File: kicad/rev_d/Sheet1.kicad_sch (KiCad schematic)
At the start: 159 parts, among them J1 JUMPER, J2 JUMPER, J3 JUMPER, J4 JUMPER, J7 JUMPER, Q1 QUARTZ, X1 FDD34M, X2 IDE40M, X3 IDC26LPT, X7 DB15VGA, X8 PLB1-4I, X9 PLB1-2

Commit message: pentevo: small update to converted kicad sch (resistors, capacitors, regulators, glue logic)
git-svn-id: svn://localhost/local-pentevo@1170 c6c76956-fad2-4150-a3a9-ea0a427205ba
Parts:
- D19: value 138 -> '138
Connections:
- net GND: now also C102.2, C103.2, C104.2, C70.2, C71.2, C79.2, C80.2, C95.2, R54.1 (i/o), R59.1 (i/o)
- net IORQGE1: now also R58.2 (i/o1)
- net IORQGE2: now also R59.2 (i/o1)
- net VCC12S: now also J4.1 (2)
- net VCC2V5: now also C28.1, C79.1, C80.1
- net VCC3V3: now also C26.1, C70.1, C71.1
- net VCC5: now also C25.1, C27.1, R48.1 (i/o), R49.1 (i/o), R51.1 (i/o), R52.1 (i/o), R64.1 (i/o)
- net ~{BUSR}: now also R53.2 (i/o1)
- net ~{CSROM}: now also R56.2 (i/o1)
- net ~{MREQ}: now also R49.2 (i/o1)
- net at C101.4: no longer C103.2
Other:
- moved on the sheet: C100, C101, C102, C95, C96, C97, C98, C99, J4, R96

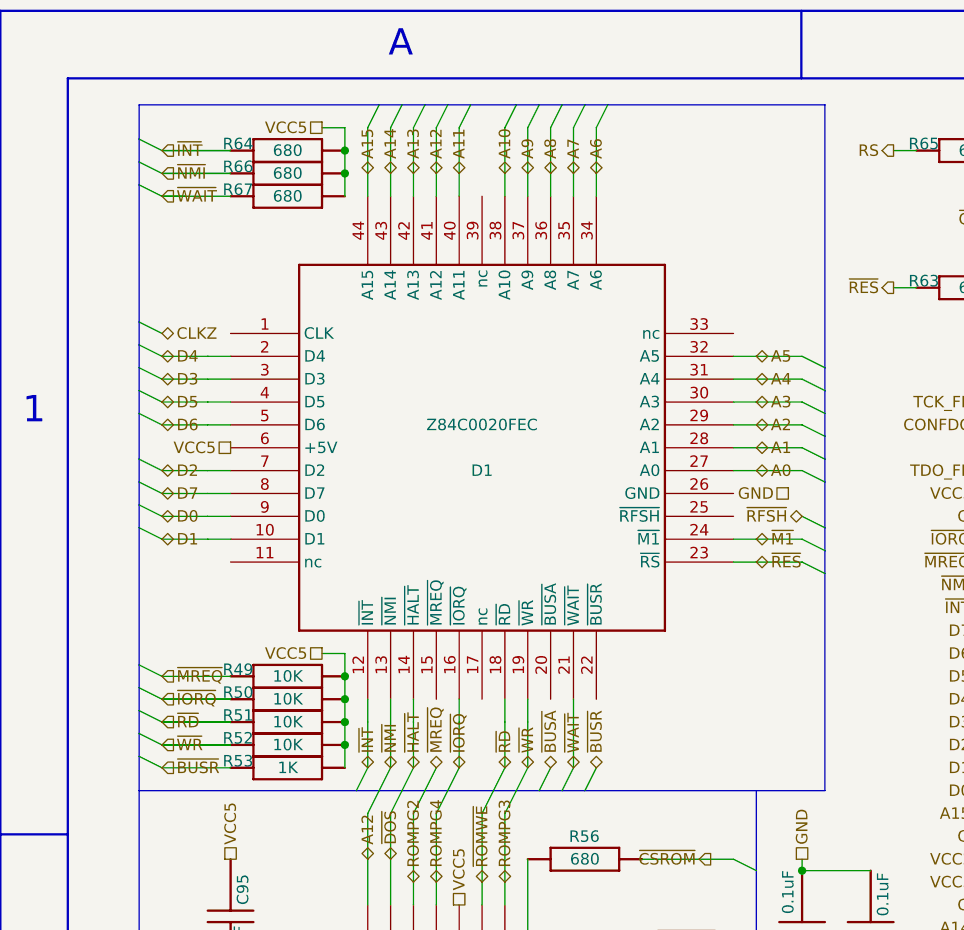
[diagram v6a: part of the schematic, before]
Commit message: pentevo: small update to converted kicad sch (Z80)
git-svn-id: svn://localhost/local-pentevo@1171 c6c76956-fad2-4150-a3a9-ea0a427205ba
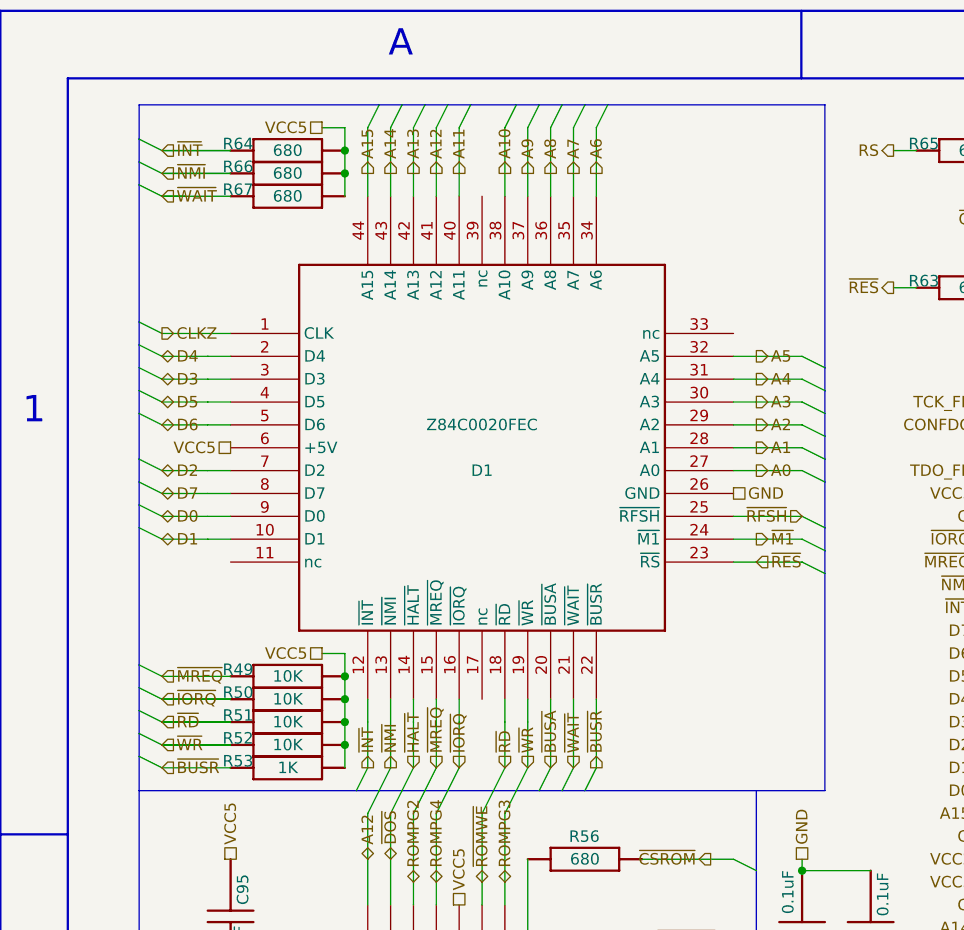
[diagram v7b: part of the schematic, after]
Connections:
- net CLKZ: now also D1.1 (CLK)
- net GND: now also D1.26 (GND)
- net ~{BUSA}: now also D1.20 (~{BUSA})
- net ~{BUSR}: now also D1.22 (~{BUSR})
- net ~{MREQ}: now also D1.15 (~{MREQ})
- net ~{RFSH}: now also D1.25 (~{RFSH})
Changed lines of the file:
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@@
 	(wire
 		(pts
+			(xy 71.12 124.46) (xy 71.12 132.08)
+		)
+		(stroke
+			(width 0)
+			(type default)
+		)
+	)
+	(wire
+		(pts
 			(xy 381 276.86) (xy 388.62 276.86)
 		)
@@
 	(wire
 		(pts
+			(xy 58.42 124.46) (xy 58.42 132.08)
+		)
+		(stroke
+			(width 0)
+			(type default)
+		)
+	)
+	(wire
+		(pts
 			(xy 63.5 322.58) (xy 68.58 322.58)
 		)
@@
 		)
 	)
+	(wire
+		(pts
+			(xy 91.44 104.14) (xy 99.06 104.14)
+		)
+		(stroke
+			(width 0)
+			(type default)
+		)
+	)
 	(bus
 		(pts
@@
 	(wire
 		(pts
+			(xy 76.2 124.46) (xy 76.2 132.08)
+		)
+		(stroke
+			(width 0)
+			(type default)
+		)
+	)
+	(wire
+		(pts
 			(xy 212.09 260.35) (xy 207.01 260.35)
 		)
@@
 	(wire
 		(pts
+			(xy 27.94 83.82) (xy 35.56 83.82)
+		)
+		(stroke
+			(width 0)
+			(type default)
+		)
+	)
+	(wire
+		(pts
 			(xy 241.3 127) (xy 246.38 127)
 		)
@@
 	)
 	(hierarchical_label "A0"
-		(shape bidirectional)
+		(shape output)
 		(at 93.98 99.06 0)
 		(fields_autoplaced yes)
@@
 	)
 	(hierarchical_label "A15"
-		(shape bidirectional)
+		(shape output)
 		(at 50.8 66.04 90)
 		(fields_autoplaced yes)
@@
 	)
 	(hierarchical_label "~{HALT}"
-		(shape bidirectional)
+		(shape input)
 		(at 55.88 132.08 90)
 		(fields_autoplaced yes)
@@
 	)
 	(hierarchical_label "A13"
-		(shape bidirectional)
+		(shape output)
 		(at 55.88 66.04 90)
 		(fields_autoplaced yes)
@@
 	)
 	(hierarchical_label "A4"
-		(shape bidirectional)
+		(shape output)
 		(at 93.98 88.9 0)
 		(fields_autoplaced yes)
@@
 	)
 	(hierarchical_label "~{BUSA}"
-		(shape bidirectional)
+		(shape input)
 		(at 71.12 132.08 90)
 		(fields_autoplaced yes)
@@
 	)
 	(hierarchical_label "~{M1}"
-		(shape bidirectional)
+		(shape output)
 		(at 93.98 106.68 0)
 		(fields_autoplaced yes)
@@
 	)
 	(hierarchical_label "A9"
-		(shape bidirectional)
+		(shape output)
 		(at 68.58 66.04 90)
 		(fields_autoplaced yes)
@@
 	)
 	(hierarchical_label "A3"
-		(shape bidirectional)
+		(shape output)
 		(at 93.98 91.44 0)
 		(fields_autoplaced yes)
@@
 	)
 	(hierarchical_label "~{INT}"
-		(shape bidirectional)
+		(shape output)
 		(at 50.8 132.08 90)
 		(fields_autoplaced yes)
@@
 	)
 	(hierarchical_label "A7"
-		(shape bidirectional)
+		(shape output)
 		(at 73.66 66.04 90)
 		(fields_autoplaced yes)
@@
 	)
 	(hierarchical_label "~{WR}"
-		(shape bidirectional)
+		(shape input)
 		(at 68.58 132.08 90)
 		(fields_autoplaced yes)
@@
 	)
 	(hierarchical_label "~{BUSR}"
-		(shape bidirectional)
+		(shape output)
 		(at 76.2 132.08 90)
 		(fields_autoplaced yes)
@@
 	)
 	(hierarchical_label "~{MREQ}"
-		(shape bidirectional)
+		(shape input)
 		(at 58.42 132.08 90)
 		(fields_autoplaced yes)
@@
 	)
 	(hierarchical_label "A6"
-		(shape bidirectional)
+		(shape output)
 		(at 76.2 66.04 90)
 		(fields_autoplaced yes)
@@
 	)
 	(hierarchical_label "~{RFSH}"
-		(shape bidirectional)
+		(shape input)
 		(at 99.06 104.14 180)
 		(fields_autoplaced yes)
@@
 	)
 	(hierarchical_label "A2"
-		(shape bidirectional)
+		(shape output)
 		(at 93.98 93.98 0)
 		(fields_autoplaced yes)
@@
 	)
 	(hierarchical_label "A12"
-		(shape bidirectional)
+		(shape output)
 		(at 58.42 66.04 90)
 		(fields_autoplaced yes)
@@
 	)
 	(hierarchical_label "A5"
-		(shape bidirectional)
+		(shape output)
 		(at 93.98 86.36 0)
 		(fields_autoplaced yes)
@@
 	)
 	(hierarchical_label "CLKZ"
-		(shape bidirectional)
+		(shape output)
 		(at 27.94 83.82 0)
 		(fields_autoplaced yes)
@@
 	)
 	(hierarchical_label "~{NMI}"
-		(shape bidirectional)
+		(shape output)
 		(at 53.34 132.08 90)
 		(fields_autoplaced yes)
@@
 	)
 	(hierarchical_label "~{WAIT}"
-		(shape bidirectional)
+		(shape input)
 		(at 73.66 132.08 90)
 		(fields_autoplaced yes)
@@
 	)
 	(hierarchical_label "A8"
-		(shape bidirectional)
+		(shape output)
 		(at 71.12 66.04 90)
 		(fields_autoplaced yes)
@@
 	)
 	(hierarchical_label "A10"
-		(shape bidirectional)
+		(shape output)
 		(at 66.04 66.04 90)
 		(fields_autoplaced yes)
@@
 	)
 	(hierarchical_label "A1"
-		(shape bidirectional)
+		(shape output)
 		(at 93.98 96.52 0)
 		(fields_autoplaced yes)
@@
 	)
 	(hierarchical_label "A11"
-		(shape bidirectional)
+		(shape output)
 		(at 60.96 66.04 90)
 		(fields_autoplaced yes)
@@
 	)
 	(hierarchical_label "~{RD}"
-		(shape bidirectional)
+		(shape input)
 		(at 66.04 132.08 90)
 		(fields_autoplaced yes)
@@
 	)
 	(hierarchical_label "A14"
-		(shape bidirectional)
+		(shape output)
 		(at 53.34 66.04 90)
 		(fields_autoplaced yes)
@@
 	(hierarchical_label "GND"
 		(shape passive)
-		(at 97.536 101.6 180)
+		(at 91.44 101.6 0)
 		(fields_autoplaced yes)
 		(effects
@@
 				(size 1.27 1.27)
 			)
-			(justify right)
+			(justify left)
 		)
 	)
@@
 	)
 	(hierarchical_label "~{RES}"
-		(shape bidirectional)
+		(shape input)
 		(at 93.98 109.22 0)
 		(fields_autoplaced yes)
@@
 	)
 	(hierarchical_label "~{IORQ}"
-		(shape bidirectional)
+		(shape input)
 		(at 60.96 132.08 90)
 		(fields_autoplaced yes)

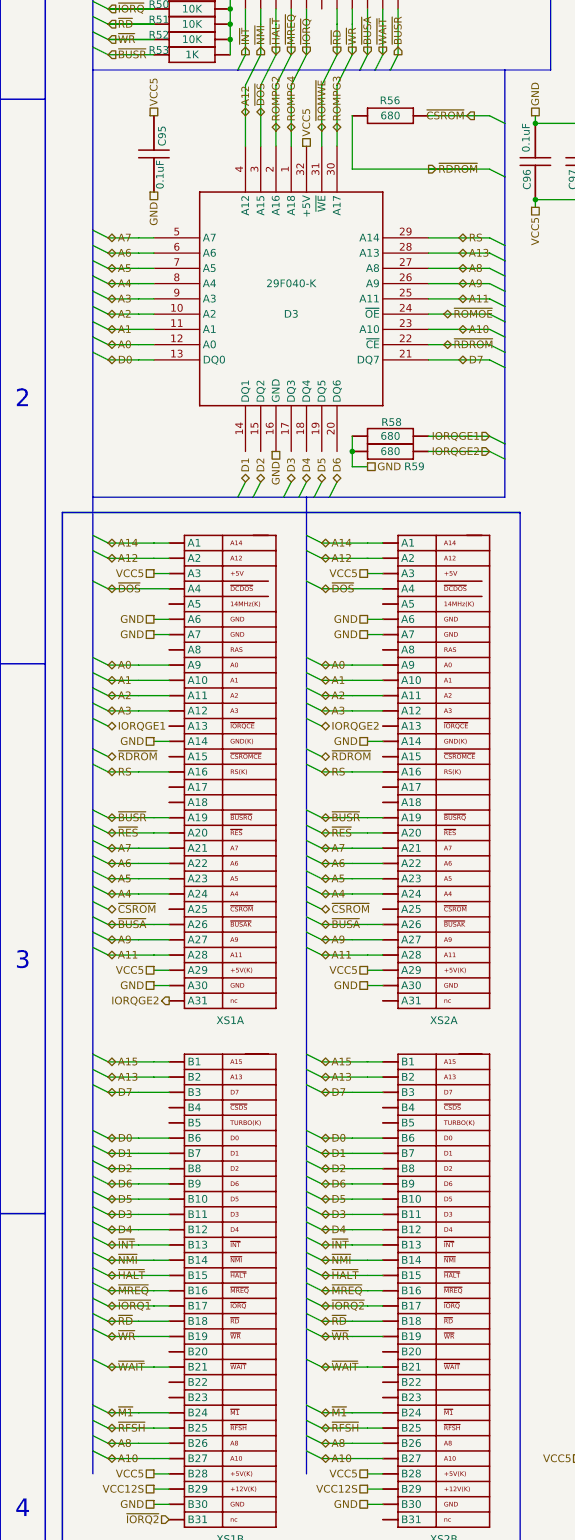
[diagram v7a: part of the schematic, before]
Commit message: pentevo: small update to converted kicad sch (flash, zxbus)
git-svn-id: svn://localhost/local-pentevo@1172 c6c76956-fad2-4150-a3a9-ea0a427205ba
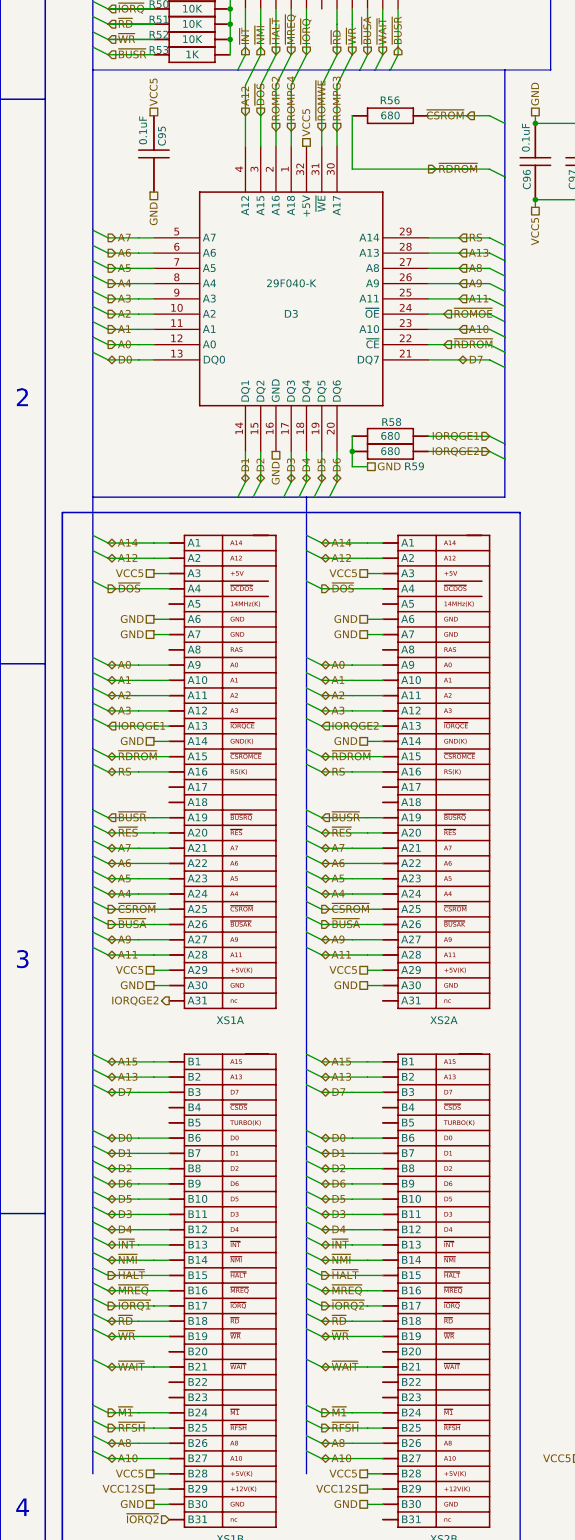
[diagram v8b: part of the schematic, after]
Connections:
- net D1: now also D3.14 (DQ1)
- net D2: now also D3.15 (DQ2)
- net D3: now also D3.17 (DQ3)
- net D4: now also D3.18 (DQ4)
- net D5: now also D3.19 (DQ5)
- net D6: now also D3.20 (DQ6)
- net IORQGE1: now also XS1.A13
- net IORQGE2: now also XS2.A13
- net ~{CSROM}: now also XS1.A25, XS2.A25
- net ~{RDROM}: now also XS1.A15, XS2.A15
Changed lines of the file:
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@@
 	(wire
 		(pts
+			(xy 63.5 243.84) (xy 73.66 243.84)
+		)
+		(stroke
+			(width 0)
+			(type default)
+		)
+	)
+	(wire
+		(pts
 			(xy 388.62 261.62) (xy 391.16 261.62)
 		)
@@
 	(wire
 		(pts
+			(xy 27.94 243.84) (xy 38.1 243.84)
+		)
+		(stroke
+			(width 0)
+			(type default)
+		)
+	)
+	(wire
+		(pts
 			(xy 209.55 227.33) (xy 212.09 227.33)
 		)
@@
 		)
 	)
+	(wire
+		(pts
+			(xy 27.94 248.92) (xy 38.1 248.92)
+		)
+		(stroke
+			(width 0)
+			(type default)
+		)
+	)
 	(bus
 		(pts
@@
 	(wire
 		(pts
+			(xy 66.04 198.12) (xy 66.04 203.2)
+		)
+		(stroke
+			(width 0)
+			(type default)
+		)
+	)
+	(wire
+		(pts
 			(xy 119.38 276.86) (xy 121.92 276.86)
 		)
@@
 	(wire
 		(pts
+			(xy 53.34 198.12) (xy 53.34 203.2)
+		)
+		(stroke
+			(width 0)
+			(type default)
+		)
+	)
+	(wire
+		(pts
 			(xy 467.36 276.86) (xy 464.82 276.86)
 		)
@@
 	(wire
 		(pts
+			(xy 60.96 198.12) (xy 60.96 203.2)
+		)
+		(stroke
+			(width 0)
+			(type default)
+		)
+	)
+	(wire
+		(pts
 			(xy 462.28 160.02) (xy 462.28 193.04)
 		)
@@
 	(wire
 		(pts
+			(xy 63.5 248.92) (xy 73.66 248.92)
+		)
+		(stroke
+			(width 0)
+			(type default)
+		)
+	)
+	(wire
+		(pts
 			(xy 241.3 86.36) (xy 246.38 86.36)
 		)
@@
 	(wire
 		(pts
+			(xy 63.5 274.32) (xy 73.66 274.32)
+		)
+		(stroke
+			(width 0)
+			(type default)
+		)
+	)
+	(wire
+		(pts
 			(xy 86.36 177.8) (xy 81.28 177.8)
 		)
@@
 	(wire
 		(pts
+			(xy 27.94 274.32) (xy 38.1 274.32)
+		)
+		(stroke
+			(width 0)
+			(type default)
+		)
+	)
+	(wire
+		(pts
 			(xy 238.76 391.16) (xy 236.22 391.16)
 		)
@@
 		)
 	)
+	(wire
+		(pts
+			(xy 63.5 198.12) (xy 63.5 203.2)
+		)
+		(stroke
+			(width 0)
+			(type default)
+		)
+	)
 	(polyline
 		(pts
@@
 	(wire
 		(pts
+			(xy 58.42 198.12) (xy 58.42 203.2)
+		)
+		(stroke
+			(width 0)
+			(type default)
+		)
+	)
+	(wire
+		(pts
 			(xy 381 289.56) (xy 388.62 289.56)
 		)
@@
 	(wire
 		(pts
+			(xy 50.8 198.12) (xy 50.8 203.2)
+		)
+		(stroke
+			(width 0)
+			(type default)
+		)
+	)
+	(wire
+		(pts
 			(xy 27.94 279.4) (xy 33.02 279.4)
 		)
@@
 	)
 	(hierarchical_label "ROMPG2"
-		(shape bidirectional)
+		(shape input)
 		(at 55.88 144.78 90)
 		(fields_autoplaced yes)
@@
 	)
 	(hierarchical_label "~{BUSA}"
-		(shape bidirectional)
+		(shape output)
 		(at 27.94 276.86 0)
 		(fields_autoplaced yes)
@@
 	)
 	(hierarchical_label "RS"
-		(shape bidirectional)
+		(shape input)
 		(at 86.36 162.56 0)
 		(fields_autoplaced yes)
@@
 	)
 	(hierarchical_label "~{DOS}"
-		(shape bidirectional)
+		(shape output)
 		(at 63.5 220.98 0)
 		(fields_autoplaced yes)
@@
 	)
 	(hierarchical_label "ROMPG3"
-		(shape bidirectional)
+		(shape input)
 		(at 66.04 144.78 90)
 		(fields_autoplaced yes)
@@
 	)
 	(hierarchical_label "A2"
-		(shape bidirectional)
+		(shape output)
 		(at 27.94 175.26 0)
 		(fields_autoplaced yes)
@@
 	)
 	(hierarchical_label "~{M1}"
-		(shape bidirectional)
+		(shape output)
 		(at 27.94 358.14 0)
 		(fields_autoplaced yes)
@@
 	)
 	(hierarchical_label "A1"
-		(shape bidirectional)
+		(shape output)
 		(at 27.94 177.8 0)
 		(fields_autoplaced yes)
@@
 	)
 	(hierarchical_label "A12"
-		(shape bidirectional)
+		(shape input)
 		(at 50.8 142.24 90)
 		(fields_autoplaced yes)
@@
 	)
 	(hierarchical_label "A13"
-		(shape bidirectional)
+		(shape input)
 		(at 86.36 165.1 0)
 		(fields_autoplaced yes)
@@
 	)
 	(hierarchical_label "A3"
-		(shape bidirectional)
+		(shape output)
 		(at 27.94 172.72 0)
 		(fields_autoplaced yes)
@@
 	)
 	(hierarchical_label "~{DOS}"
-		(shape bidirectional)
+		(shape input)
 		(at 53.34 142.24 90)
 		(fields_autoplaced yes)
@@
 	)
 	(hierarchical_label "A8"
-		(shape bidirectional)
+		(shape input)
 		(at 86.36 167.64 0)
 		(fields_autoplaced yes)
@@
 	)
 	(hierarchical_label "A0"
-		(shape bidirectional)
+		(shape output)
 		(at 27.94 180.34 0)
 		(fields_autoplaced yes)
@@
 	)
 	(hierarchical_label "~{RDROM}"
-		(shape bidirectional)
+		(shape input)
 		(at 83.82 180.34 0)
 		(fields_autoplaced yes)
@@
 	)
 	(hierarchical_label "~{CSROM}"
-		(shape bidirectional)
+		(shape output)
 		(at 63.5 274.32 0)
 		(fields_autoplaced yes)
@@
 	)
 	(hierarchical_label "A4"
-		(shape bidirectional)
+		(shape output)
 		(at 27.94 170.18 0)
 		(fields_autoplaced yes)
@@
 	)
 	(hierarchical_label "IORQGE1"
-		(shape bidirectional)
+		(shape input)
 		(at 27.94 243.84 0)
 		(fields_autoplaced yes)
@@
 	)
 	(hierarchical_label "~{BUSA}"
-		(shape bidirectional)
+		(shape output)
 		(at 63.5 276.86 0)
 		(fields_autoplaced yes)
@@
 	)
 	(hierarchical_label "~{IORQ1}"
-		(shape bidirectional)
+		(shape output)
 		(at 27.94 340.36 0)
 		(fields_autoplaced yes)
@@
 	)
 	(hierarchical_label "~{BUSR}"
-		(shape bidirectional)
+		(shape input)
 		(at 63.5 259.08 0)
 		(fields_autoplaced yes)
@@
 	)
 	(hierarchical_label "~{RFSH}"
-		(shape bidirectional)
+		(shape output)
 		(at 63.5 360.68 0)
 		(fields_autoplaced yes)
@@
 	)
 	(hierarchical_label "A7"
-		(shape bidirectional)
+		(shape output)
 		(at 27.94 162.56 0)
 		(fields_autoplaced yes)
@@
 	)
 	(hierarchical_label "~{ROMOE}"
-		(shape bidirectional)
+		(shape input)
 		(at 83.82 175.26 0)
 		(fields_autoplaced yes)
@@
 	)
 	(hierarchical_label "A5"
-		(shape bidirectional)
+		(shape output)
 		(at 27.94 167.64 0)
 		(fields_autoplaced yes)
@@
 	)
 	(hierarchical_label "~{RFSH}"
-		(shape bidirectional)
+		(shape output)
 		(at 27.94 360.68 0)
 		(fields_autoplaced yes)
@@
 	)
 	(hierarchical_label "~{M1}"
-		(shape bidirectional)
+		(shape output)
 		(at 63.5 358.14 0)
 		(fields_autoplaced yes)
@@
 	)
 	(hierarchical_label "~{HALT}"
-		(shape bidirectional)
+		(shape output)
 		(at 27.94 335.28 0)
 		(fields_autoplaced yes)
@@
 	)
 	(hierarchical_label "A6"
-		(shape bidirectional)
+		(shape output)
 		(at 27.94 165.1 0)
 		(fields_autoplaced yes)
@@
 	)
 	(hierarchical_label "~{BUSR}"
-		(shape bidirectional)
+		(shape input)
 		(at 27.94 259.08 0)
 		(fields_autoplaced yes)
@@
 	)
 	(hierarchical_label "ROMPG4"
-		(shape bidirectional)
+		(shape input)
 		(at 58.42 144.78 90)
 		(fields_autoplaced yes)
@@
 	)
 	(hierarchical_label "~{ROMWE}"
-		(shape bidirectional)
+		(shape input)
 		(at 63.5 144.78 90)
 		(fields_autoplaced yes)
@@
 	)
 	(hierarchical_label "A10"
-		(shape bidirectional)
+		(shape input)
 		(at 86.36 177.8 0)
 		(fields_autoplaced yes)
@@
 	)
 	(hierarchical_label "A9"
-		(shape bidirectional)
+		(shape input)
 		(at 86.36 170.18 0)
 		(fields_autoplaced yes)
@@
 	)
 	(hierarchical_label "~{IORQ2}"
-		(shape bidirectional)
+		(shape output)
 		(at 63.5 340.36 0)
 		(fields_autoplaced yes)
@@
 	)
 	(hierarchical_label "IORQGE2"
-		(shape bidirectional)
+		(shape input)
 		(at 63.5 243.84 0)
 		(fields_autoplaced yes)
@@
 	)
 	(hierarchical_label "~{CSROM}"
-		(shape bidirectional)
+		(shape output)
 		(at 27.94 274.32 0)
 		(fields_autoplaced yes)
@@
 	)
 	(hierarchical_label "~{HALT}"
-		(shape bidirectional)
+		(shape output)
 		(at 63.5 335.28 0)
 		(fields_autoplaced yes)
@@
 	)
 	(hierarchical_label "~{DOS}"
-		(shape bidirectional)
+		(shape output)
 		(at 27.94 220.98 0)
 		(fields_autoplaced yes)
@@
 	)
 	(hierarchical_label "A11"
-		(shape bidirectional)
+		(shape input)
 		(at 86.36 172.72 0)
 		(fields_autoplaced yes)
@@
 		)
 		(property "ALTIUM_VALUE" "0.1uF"
-			(at 37.338 149.606 0)
+			(at 34.544 142.24 0)
 			(effects
 				(font
